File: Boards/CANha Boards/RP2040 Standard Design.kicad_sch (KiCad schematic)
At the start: 38 parts, among them J16 DX07S016JA1R1500, J7 BM03B-SRSS-TBLFSN, U18 ST1L05APU33R, U2 ESD7L5.0DT5G, U6 W25Q128JVSIQ TR

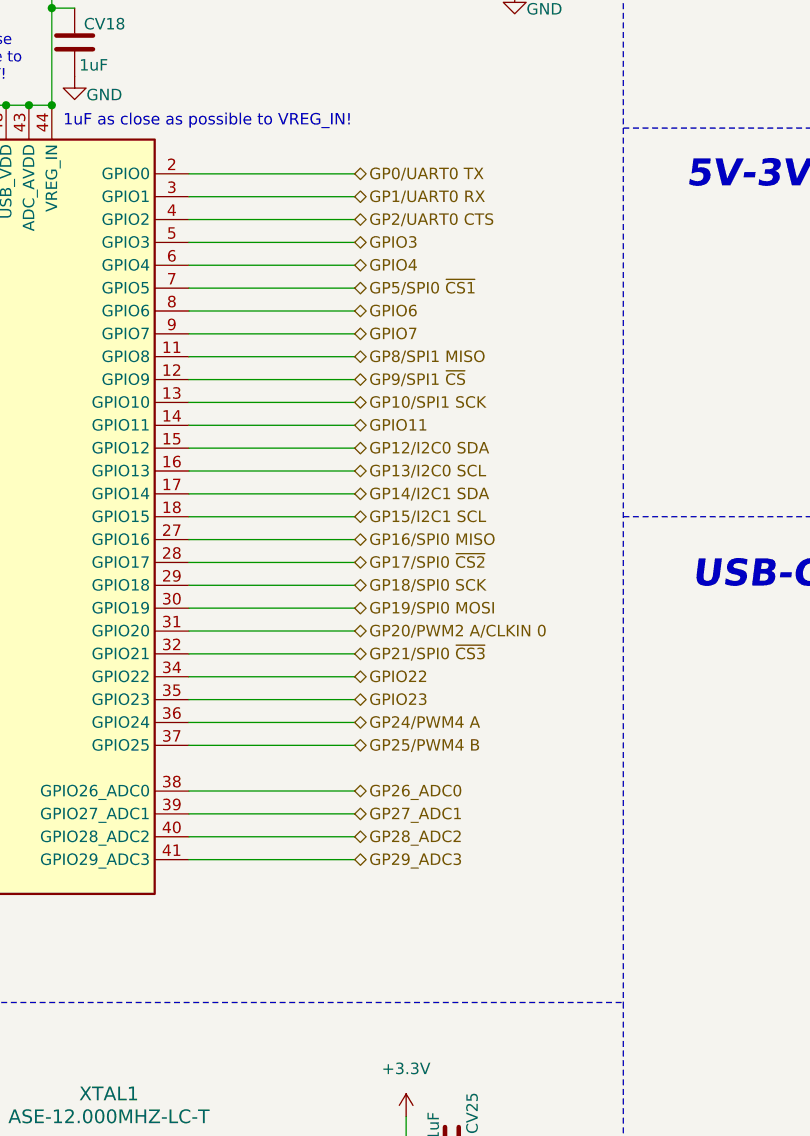
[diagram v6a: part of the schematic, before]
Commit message: changes in RP2040 design
GPIO25 LED is now part of RP2040 Standard
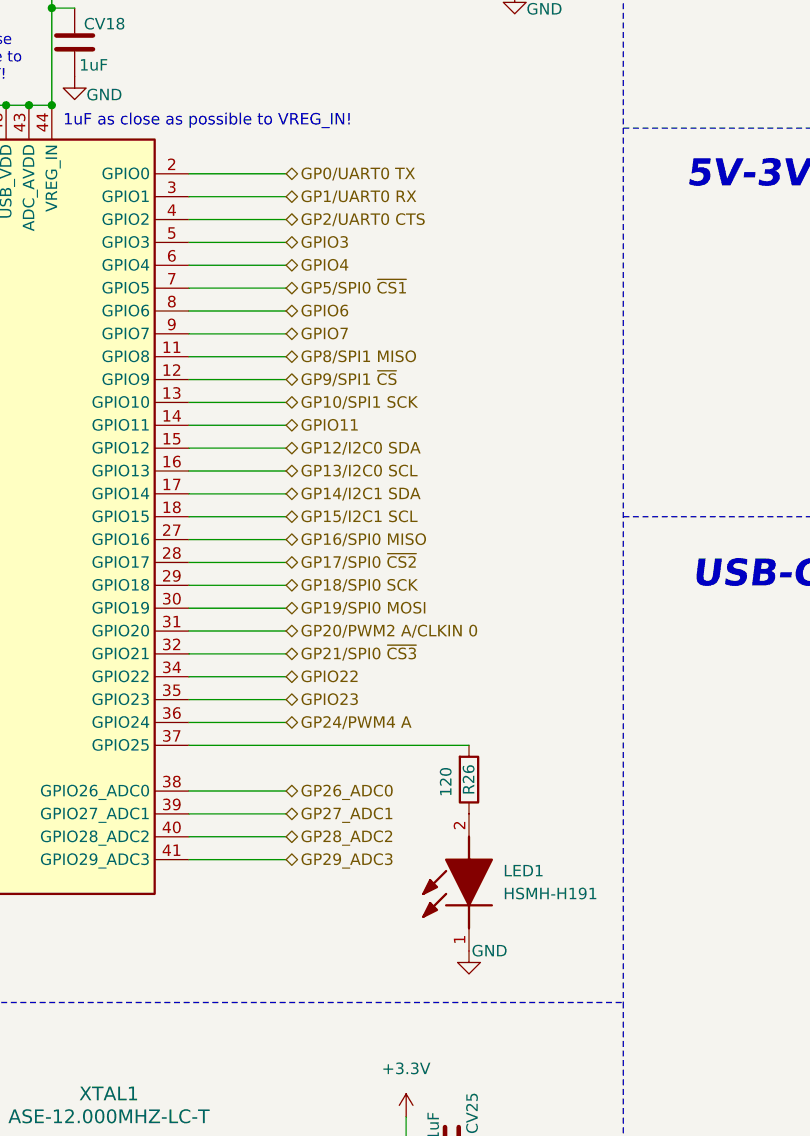
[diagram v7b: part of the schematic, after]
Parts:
- added LED1: HSMH-H191, Red SMD LED:HSMHH191, symbol Red SMD LED:HSMH-H191
- added R26: 120, RES_0402:RES_0402, symbol Device:R
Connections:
- net GND: now also LED1.1 (K)
- net GP25/PWM4 B: no longer names the net of MCU2.37 (GPIO25)
- net GP25/PWM4 B: now also R26.2
- new net: LED1.2 (A), R26.1
